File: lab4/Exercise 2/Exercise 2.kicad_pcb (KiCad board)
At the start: 2 copper layers, 22.9 x 29 mm, 10 parts, among them J1 Conn_01x02_Male, U1 NE555D

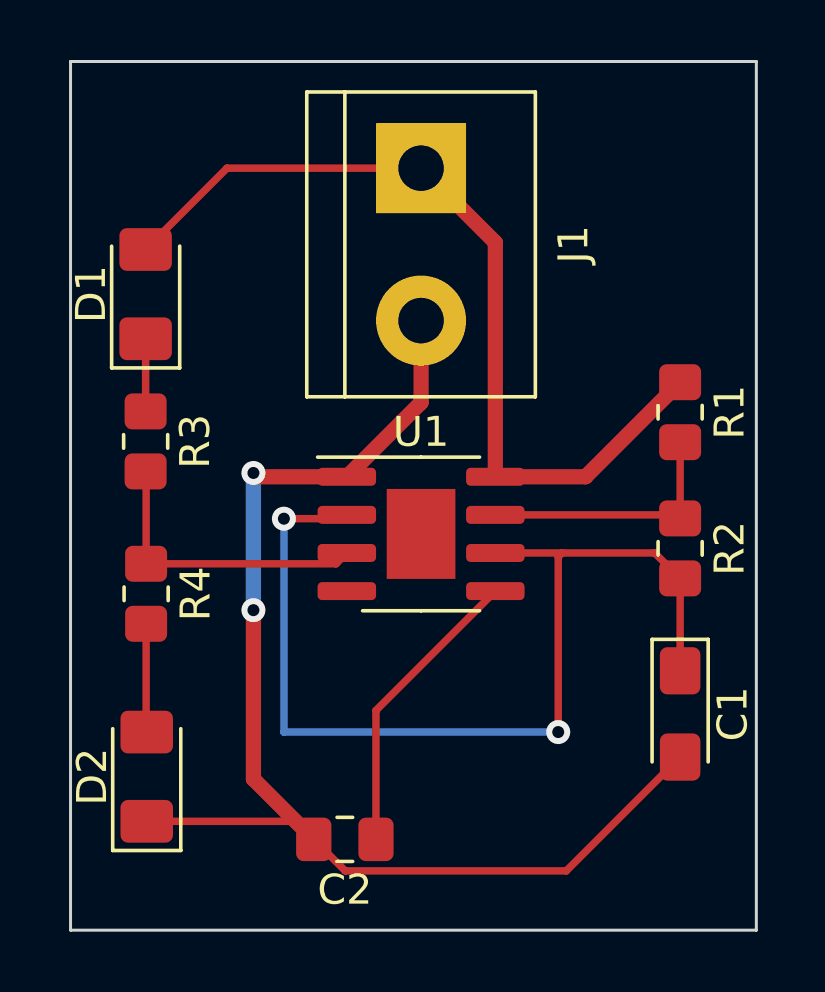
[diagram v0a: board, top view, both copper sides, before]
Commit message: finished arduometer build
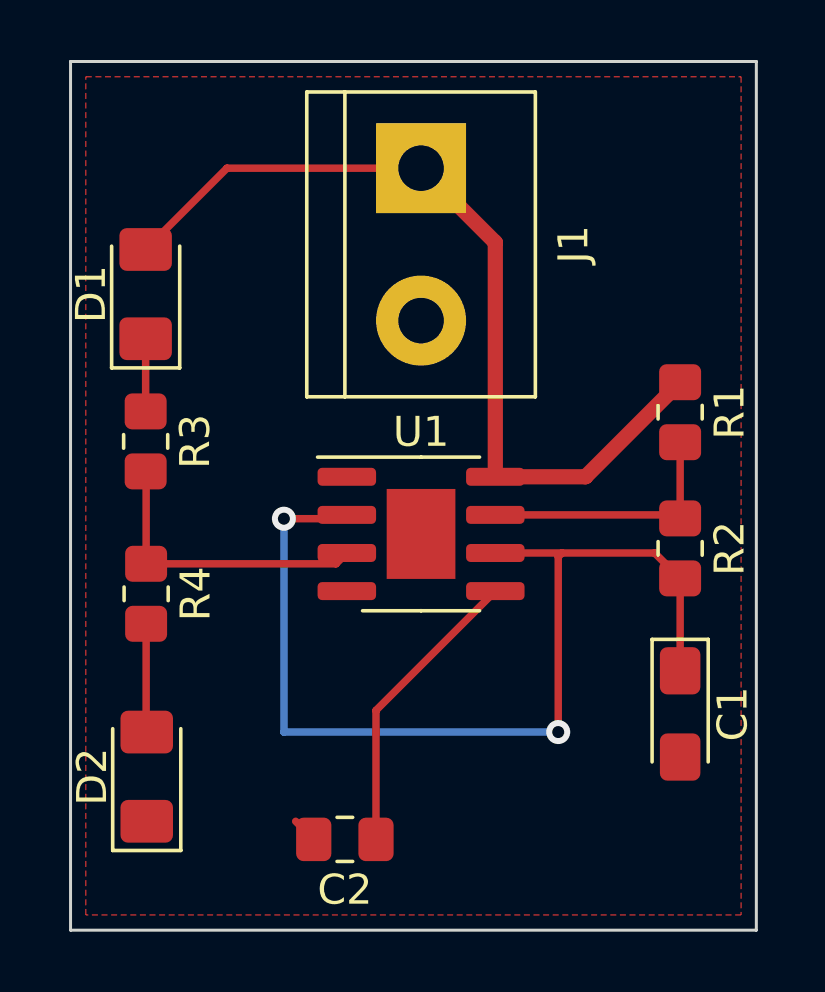
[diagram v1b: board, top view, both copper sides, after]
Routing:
- net GND: track 42.5 -> 0.85 mm, vias 2 -> 0
- added copper zone on F.Cu, net GND
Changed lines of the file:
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@@
       (outputformat 1)
       (mirror false)
-      (drillshape 1)
+      (drillshape 0)
       (scaleselection 1)
-      (outputdirectory "")
+      (outputdirectory "Ex 2 Gerber/")
     )
   )
@@
     (fp_line (start -1 -0.625) (end 1 -0.625) (layer "F.Fab") (width 0.1))
     (fp_line (start 1 -0.625) (end 1 0.625) (layer "F.Fab") (width 0.1))
-    (pad "1" smd roundrect (at -1 0 270) (size 1.2 1.4) (layers "F.Cu" "F.Paste" "F.Mask") (roundrect_rratio 0.208333)
+    (pad "1" smd roundrect (at -1 0 270) (size 1.2 1.4) (layers "F.Cu" "F.Paste" "F.Mask") (roundrect_rratio 0.2083333333)
       (net 4 "Net-(D1-Pad1)") (pintype "passive"))
-    (pad "2" smd roundrect (at 1 0 270) (size 1.2 1.4) (layers "F.Cu" "F.Paste" "F.Mask") (roundrect_rratio 0.208333)
+    (pad "2" smd roundrect (at 1 0 270) (size 1.2 1.4) (layers "F.Cu" "F.Paste" "F.Mask") (roundrect_rratio 0.2083333333)
       (net 8 "/pin_3") (pintype "passive"))
     (model "${KICAD6_3DMODEL_DIR}/Resistor_SMD.3dshapes/R_0805_2012Metric.wrl"
@@
     (fp_line (start -1.2 -0.8) (end -1.6 -0.4) (layer "F.Fab") (width 0.1))
     (fp_line (start 1.6 0.8) (end 1.6 -0.8) (layer "F.Fab") (width 0.1))
-    (pad "1" smd roundrect (at -1.4375 0 270) (size 1.575 1.35) (layers "F.Cu" "F.Paste" "F.Mask") (roundrect_rratio 0.185185)
+    (pad "1" smd roundrect (at -1.4375 0 270) (size 1.575 1.35) (layers "F.Cu" "F.Paste" "F.Mask") (roundrect_rratio 0.1851851852)
       (net 1 "/pin_2") (pintype "passive"))
-    (pad "2" smd roundrect (at 1.4375 0 270) (size 1.575 1.35) (layers "F.Cu" "F.Paste" "F.Mask") (roundrect_rratio 0.185185)
+    (pad "2" smd roundrect (at 1.4375 0 270) (size 1.575 1.35) (layers "F.Cu" "F.Paste" "F.Mask") (roundrect_rratio 0.1851851852)
       (net 2 "GND") (pintype "passive"))
     (model "${KICAD6_3DMODEL_DIR}/Capacitor_Tantalum_SMD.3dshapes/CP_EIA-3216-18_Kemet-A.wrl"
@@
     (fp_line (start 1 0.625) (end -1 0.625) (layer "F.Fab") (width 0.1))
     (fp_line (start -1 0.625) (end -1 -0.625) (layer "F.Fab") (width 0.1))
-    (pad "1" smd roundrect (at -1 0 270) (size 1.2 1.4) (layers "F.Cu" "F.Paste" "F.Mask") (roundrect_rratio 0.208333)
+    (pad "1" smd roundrect (at -1 0 270) (size 1.2 1.4) (layers "F.Cu" "F.Paste" "F.Mask") (roundrect_rratio 0.2083333333)
       (net 7 "Net-(R1-Pad2)") (pintype "passive"))
-    (pad "2" smd roundrect (at 1 0 270) (size 1.2 1.4) (layers "F.Cu" "F.Paste" "F.Mask") (roundrect_rratio 0.208333)
+    (pad "2" smd roundrect (at 1 0 270) (size 1.2 1.4) (layers "F.Cu" "F.Paste" "F.Mask") (roundrect_rratio 0.2083333333)
       (net 1 "/pin_2") (pintype "passive"))
     (model "${KICAD6_3DMODEL_DIR}/Resistor_SMD.3dshapes/R_0805_2012Metric.wrl"
@@
     (fp_line (start -1 -0.625) (end 1 -0.625) (layer "F.Fab") (width 0.1))
     (fp_line (start 1 0.625) (end -1 0.625) (layer "F.Fab") (width 0.1))
-    (pad "1" smd roundrect (at -1 0 270) (size 1.2 1.4) (layers "F.Cu" "F.Paste" "F.Mask") (roundrect_rratio 0.208333)
+    (pad "1" smd roundrect (at -1 0 270) (size 1.2 1.4) (layers "F.Cu" "F.Paste" "F.Mask") (roundrect_rratio 0.2083333333)
       (net 8 "/pin_3") (pintype "passive"))
-    (pad "2" smd roundrect (at 1 0 270) (size 1.2 1.4) (layers "F.Cu" "F.Paste" "F.Mask") (roundrect_rratio 0.208333)
+    (pad "2" smd roundrect (at 1 0 270) (size 1.2 1.4) (layers "F.Cu" "F.Paste" "F.Mask") (roundrect_rratio 0.2083333333)
       (net 6 "Net-(D2-Pad2)") (pintype "passive"))
     (model "${KICAD6_3DMODEL_DIR}/Resistor_SMD.3dshapes/R_0805_2012Metric.wrl"
@@
     (fp_line (start -1 0.625) (end -1 -0.625) (layer "F.Fab") (width 0.1))
     (fp_line (start 1 -0.625) (end 1 0.625) (layer "F.Fab") (width 0.1))
-    (pad "1" smd roundrect (at -1 0 270) (size 1.2 1.4) (layers "F.Cu" "F.Paste" "F.Mask") (roundrect_rratio 0.208333)
+    (pad "1" smd roundrect (at -1 0 270) (size 1.2 1.4) (layers "F.Cu" "F.Paste" "F.Mask") (roundrect_rratio 0.2083333333)
       (net 5 "+9V") (pintype "passive"))
-    (pad "2" smd roundrect (at 1 0 270) (size 1.2 1.4) (layers "F.Cu" "F.Paste" "F.Mask") (roundrect_rratio 0.208333)
+    (pad "2" smd roundrect (at 1 0 270) (size 1.2 1.4) (layers "F.Cu" "F.Paste" "F.Mask") (roundrect_rratio 0.2083333333)
       (net 7 "Net-(R1-Pad2)") (pintype "passive"))
     (model "${KICAD6_3DMODEL_DIR}/Resistor_SMD.3dshapes/R_0805_2012Metric.wrl"
@@
     (fp_line (start -1 -0.625) (end 1 -0.625) (layer "F.Fab") (width 0.1))
     (fp_line (start -1 0.625) (end -1 -0.625) (layer "F.Fab") (width 0.1))
-    (pad "1" smd roundrect (at -1.0375 0 180) (size 1.175 1.45) (layers "F.Cu" "F.Paste" "F.Mask") (roundrect_rratio 0.212766)
+    (pad "1" smd roundrect (at -1.0375 0 180) (size 1.175 1.45) (layers "F.Cu" "F.Paste" "F.Mask") (roundrect_rratio 0.2127659574)
       (net 3 "Net-(C2-Pad1)") (pintype "passive"))
-    (pad "2" smd roundrect (at 1.0375 0 180) (size 1.175 1.45) (layers "F.Cu" "F.Paste" "F.Mask") (roundrect_rratio 0.212766)
+    (pad "2" smd roundrect (at 1.0375 0 180) (size 1.175 1.45) (layers "F.Cu" "F.Paste" "F.Mask") (roundrect_rratio 0.2127659574)
       (net 2 "GND") (pintype "passive"))
     (model "${KICAD6_3DMODEL_DIR}/Capacitor_SMD.3dshapes/C_0805_2012Metric.wrl"
@@
     (fp_line (start -1.2 -0.8) (end -1.6 -0.4) (layer "F.Fab") (width 0.1))
     (fp_line (start 1.6 0.8) (end 1.6 -0.8) (layer "F.Fab") (width 0.1))
-    (pad "1" smd roundrect (at -1.4875 0 90) (size 1.425 1.75) (layers "F.Cu" "F.Paste" "F.Mask") (roundrect_rratio 0.175439)
+    (pad "1" smd roundrect (at -1.4875 0 90) (size 1.425 1.75) (layers "F.Cu" "F.Paste" "F.Mask") (roundrect_rratio 0.1754392982)
       (net 2 "GND") (pinfunction "K") (pintype "passive"))
-    (pad "2" smd roundrect (at 1.4875 0 90) (size 1.425 1.75) (layers "F.Cu" "F.Paste" "F.Mask") (roundrect_rratio 0.175439)
+    (pad "2" smd roundrect (at 1.4875 0 90) (size 1.425 1.75) (layers "F.Cu" "F.Paste" "F.Mask") (roundrect_rratio 0.1754392982)
       (net 6 "Net-(D2-Pad2)") (pinfunction "A") (pintype "passive"))
     (model "${KICAD6_3DMODEL_DIR}/LED_SMD.3dshapes/LED_1206_3216Metric.wrl"
@@
     (fp_line (start -1.6 0.8) (end 1.6 0.8) (layer "F.Fab") (width 0.1))
     (fp_line (start 1.6 0.8) (end 1.6 -0.8) (layer "F.Fab") (width 0.1))
-    (pad "1" smd roundrect (at -1.4875 0 90) (size 1.425 1.75) (layers "F.Cu" "F.Paste" "F.Mask") (roundrect_rratio 0.175439)
+    (pad "1" smd roundrect (at -1.4875 0 90) (size 1.425 1.75) (layers "F.Cu" "F.Paste" "F.Mask") (roundrect_rratio 0.1754392982)
       (net 4 "Net-(D1-Pad1)") (pinfunction "K") (pintype "passive"))
-    (pad "2" smd roundrect (at 1.4875 0 90) (size 1.425 1.75) (layers "F.Cu" "F.Paste" "F.Mask") (roundrect_rratio 0.175439)
+    (pad "2" smd roundrect (at 1.4875 0 90) (size 1.425 1.75) (layers "F.Cu" "F.Paste" "F.Mask") (roundrect_rratio 0.1754392982)
       (net 5 "+9V") (pinfunction "A") (pintype "passive"))
     (model "${KICAD6_3DMODEL_DIR}/LED_SMD.3dshapes/LED_1206_3216Metric.wrl"
@@
   (segment (start 143.764 99.568) (end 143.764 92.456) (width 0.25) (layer "B.Cu") (net 1))
   (segment (start 152.908 99.568) (end 143.764 99.568) (width 0.25) (layer "B.Cu") (net 1))
-  (segment (start 153.1775 104.1955) (end 145.8085 104.1955) (width 0.25) (layer "F.Cu") (net 2))
-  (segment (start 142.748 101.135) (end 144.7585 103.1455) (width 0.508) (layer "F.Cu") (net 2))
-  (segment (start 142.875 91.059) (end 142.748 90.932) (width 0.508) (layer "F.Cu") (net 2))
-  (segment (start 142.748 95.504) (end 142.748 101.135) (width 0.508) (layer "F.Cu") (net 2))
-  (segment (start 156.972 100.401) (end 153.1775 104.1955) (width 0.25) (layer "F.Cu") (net 2))
-  (segment (start 144.156 102.543) (end 139.192 102.543) (width 0.25) (layer "F.Cu") (net 2))
-  (segment (start 145.8085 104.1955) (end 144.7585 103.1455) (width 0.25) (layer "F.Cu") (net 2))
   (segment (start 144.7585 103.1455) (end 144.156 102.543) (width 0.25) (layer "F.Cu") (net 2))
-  (segment (start 148.336 85.852) (end 148.336 88.584) (width 0.508) (layer "F.Cu") (net 2))
-  (segment (start 145.861 91.059) (end 142.875 91.059) (width 0.508) (layer "F.Cu") (net 2))
-  (segment (start 148.336 88.584) (end 145.861 91.059) (width 0.508) (layer "F.Cu") (net 2))
-  (via (at 142.748 90.932) (size 0.8) (drill 0.4) (layers "F.Cu" "B.Cu") (net 2))
-  (via (at 142.748 95.504) (size 0.8) (drill 0.4) (layers "F.Cu" "B.Cu") (net 2))
-  (segment (start 142.748 90.932) (end 142.748 95.504) (width 0.508) (layer "B.Cu") (net 2))
   (segment (start 146.8335 98.8465) (end 150.811 94.869) (width 0.25) (layer "F.Cu") (net 3))
   (segment (start 146.8335 103.1455) (end 146.8335 98.8465) (width 0.25) (layer "F.Cu") (net 3))
@@
   (segment (start 139.1715 93.9595) (end 145.5005 93.9595) (width 0.25) (layer "F.Cu") (net 8))
   (segment (start 139.1715 93.9595) (end 139.1715 90.8955) (width 0.25) (layer "F.Cu") (net 8))
+  (zone (net 2) (net_name "GND") (layer "F.Cu") (hatch edge 0.508)
+    (connect_pads (clearance 0.508))
+    (min_thickness 0.254) (filled_areas_thickness no)
+    (fill yes (thermal_gap 0.508) (thermal_bridge_width 0.508))
+    (polygon
+      (pts
+        (xy 159.004 105.664)
+        (xy 137.16 105.664)
+        (xy 137.16 77.724)
+        (xy 159.004 77.724)
+      )
+    )
+  )
 )
